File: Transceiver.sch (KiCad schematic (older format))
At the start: 13 parts

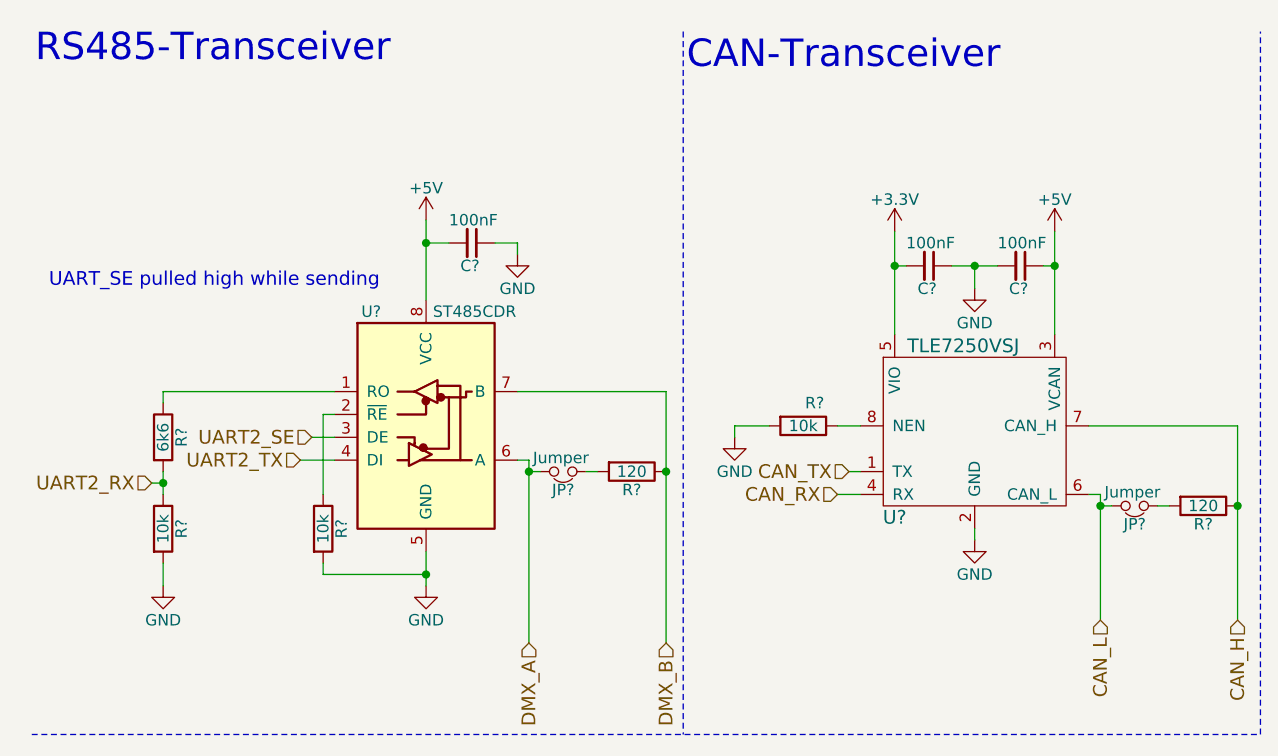
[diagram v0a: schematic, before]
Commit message: Unmerged the LED-Parts
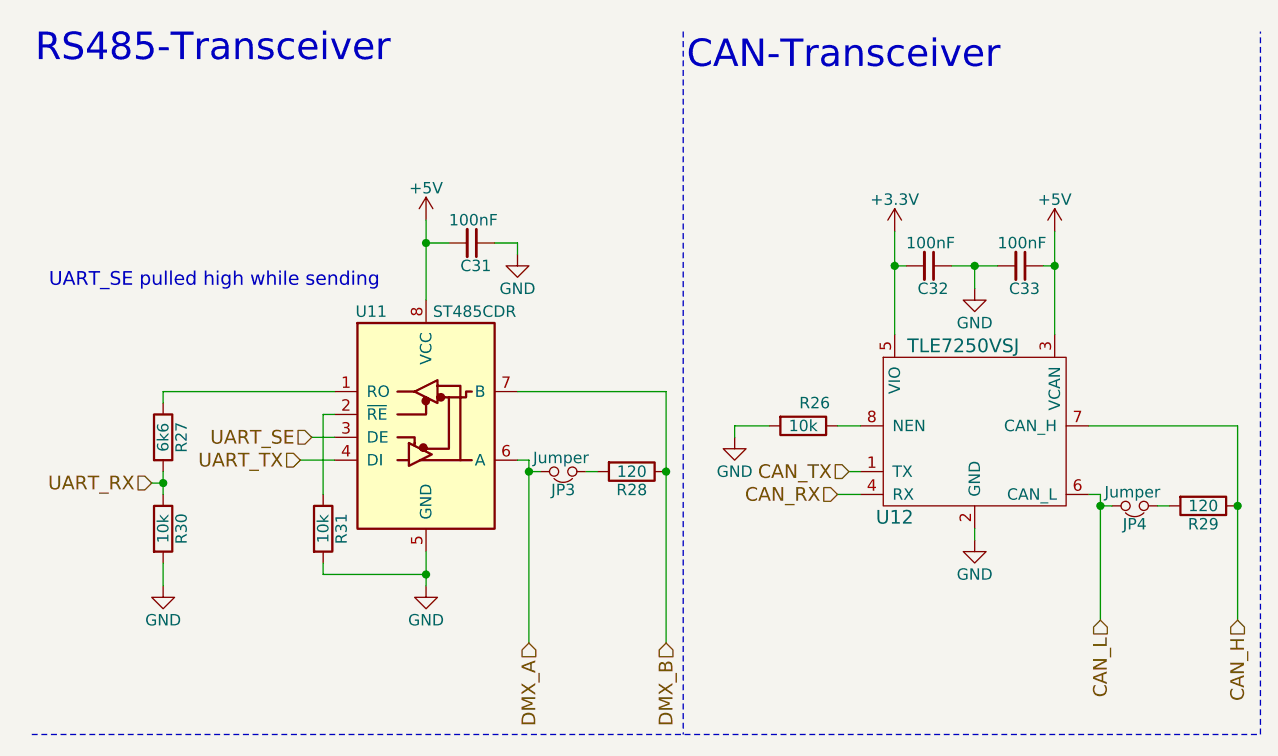
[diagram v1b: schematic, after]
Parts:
- C28, C29, C30: renamed from C?; footprint (none) -> Capacitors_SMD:C_0603
- R20, R21, R22, R23, R24, R25: renamed from R?; footprint (none) -> Resistors_SMD:R_0603
- gave numbers to parts that had none: 4
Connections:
- net UART2_RX renamed UART_RX
- net UART2_SE renamed UART_SE
- net UART2_TX renamed UART_TX
